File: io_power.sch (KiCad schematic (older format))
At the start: 21 parts, among them U11 TPS7A7100, U12 TPS7A7100, U5 TCA6424A, U6 TPS7A7100

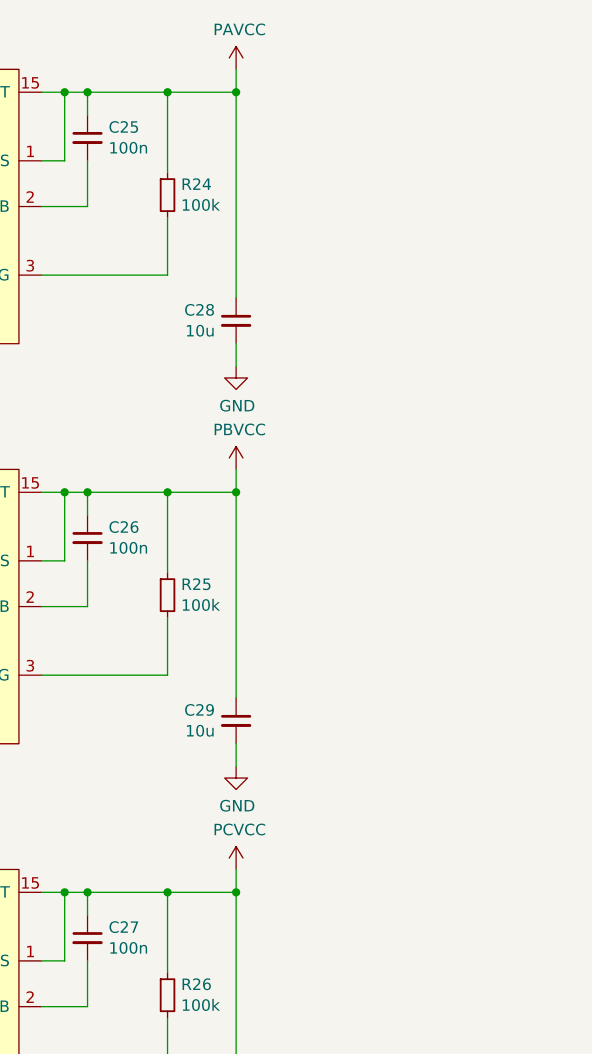
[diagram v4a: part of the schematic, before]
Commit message: Misc silk fixes and add power header
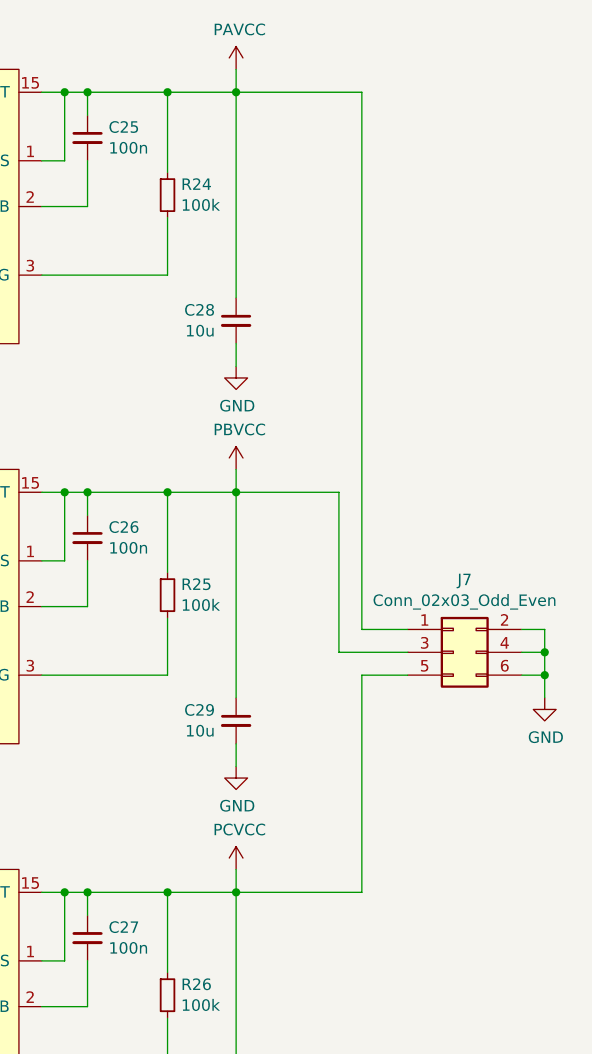
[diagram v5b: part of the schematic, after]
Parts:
- added J7: Conn_02x03_Odd_Even, Connector_PinHeader_2.54mm:PinHeader_2x03_P2.54mm_Vertical, symbol Connector_Generic:Conn_02x03_Odd_Even
- U11, U12, U6: footprint Package_DFN_QFN:VQFN-16-1EP_3x3mm_P0.5mm_EP1.6x1.6mm_ThermalVias -> antboard:VQFN-16-1EP_3x3mm_P0.5mm_EP1.6x1.6mm_ThermalVias
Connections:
- net GND: now also J7.2 (Pin_2), J7.4 (Pin_4), J7.6 (Pin_6)
- net PAVCC: now also J7.1 (Pin_1)
- net PBVCC: now also J7.3 (Pin_3)
- net PCVCC: now also J7.5 (Pin_5)
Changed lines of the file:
@@
 F 0 "U6" H 8000 1265 50  0000 C CNN
 F 1 "TPS7A7100" H 8000 1174 50  0000 C CNN
-F 2 "Package_DFN_QFN:VQFN-16-1EP_3x3mm_P0.5mm_EP1.6x1.6mm_ThermalVias" H 7650 1100 50  0001 C CNN
+F 2 "antboard:VQFN-16-1EP_3x3mm_P0.5mm_EP1.6x1.6mm_ThermalVias" H 7650 1100 50  0001 C CNN
 F 3 "https://www.ti.com/lit/ds/symlink/tps7a7100.pdf" H 7650 1100 50  0001 C CNN
 	1    7650 1100
@@
 F 0 "U11" H 8000 3015 50  0000 C CNN
 F 1 "TPS7A7100" H 8000 2924 50  0000 C CNN
-F 2 "Package_DFN_QFN:VQFN-16-1EP_3x3mm_P0.5mm_EP1.6x1.6mm_ThermalVias" H 7650 2850 50  0001 C CNN
+F 2 "antboard:VQFN-16-1EP_3x3mm_P0.5mm_EP1.6x1.6mm_ThermalVias" H 7650 2850 50  0001 C CNN
 F 3 "https://www.ti.com/lit/ds/symlink/tps7a7100.pdf" H 7650 2850 50  0001 C CNN
 	1    7650 2850
@@
 F 0 "U12" H 8000 4765 50  0000 C CNN
 F 1 "TPS7A7100" H 8000 4674 50  0000 C CNN
-F 2 "Package_DFN_QFN:VQFN-16-1EP_3x3mm_P0.5mm_EP1.6x1.6mm_ThermalVias" H 7650 4600 50  0001 C CNN
+F 2 "antboard:VQFN-16-1EP_3x3mm_P0.5mm_EP1.6x1.6mm_ThermalVias" H 7650 4600 50  0001 C CNN
 F 3 "https://www.ti.com/lit/ds/symlink/tps7a7100.pdf" H 7650 4600 50  0001 C CNN
 	1    7650 4600
@@
 NoConn ~ 4500 4650
 NoConn ~ 4500 4750
+$Comp
+L Connector_Generic:Conn_02x03_Odd_Even J7
+U 1 1 5E0E1804
+P 10250 3650
+F 0 "J7" H 10300 3967 50  0000 C CNN
+F 1 "Conn_02x03_Odd_Even" H 10300 3876 50  0000 C CNN
+F 2 "Connector_PinHeader_2.54mm:PinHeader_2x03_P2.54mm_Vertical" H 10250 3650 50  0001 C CNN
+F 3 "~" H 10250 3650 50  0001 C CNN
+	1    10250 3650
+	1    0    0    -1
+$EndComp
+$Comp
+L power:GND #PWR?
+U 1 1 5E0E2934
+P 10650 3850
+AR Path="/5E0E2934" Ref="#PWR?"  Part="1"
+AR Path="/5DF7E971/5E0E2934" Ref="#PWR?"  Part="1"
+AR Path="/5DFC2583/5E0E2934" Ref="#PWR?"  Part="1"
+AR Path="/5EA8F1AB/5E0E2934" Ref="#PWR047"  Part="1"
+F 0 "#PWR047" H 10650 3600 50  0001 C CNN
+F 1 "GND" H 10655 3677 50  0000 C CNN
+F 2 "" H 10650 3850 50  0001 C CNN
+F 3 "" H 10650 3850 50  0001 C CNN
+	1    10650 3850
+	1    0    0    -1
+$EndComp
+Wire Wire Line
+	10550 3550 10650 3550
+Wire Wire Line
+	10650 3550 10650 3650
+Wire Wire Line
+	10550 3650 10650 3650
+Connection ~ 10650 3650
+Wire Wire Line
+	10650 3650 10650 3750
+Wire Wire Line
+	10550 3750 10650 3750
+Connection ~ 10650 3750
+Wire Wire Line
+	10650 3750 10650 3850
+Wire Wire Line
+	10050 3550 9850 3550
+Wire Wire Line
+	9850 3550 9850 1200
+Wire Wire Line
+	9850 1200 9300 1200
+Wire Wire Line
+	9300 2950 9750 2950
+Wire Wire Line
+	9750 2950 9750 3650
+Wire Wire Line
+	9750 3650 10050 3650
+Wire Wire Line
+	9300 4700 9850 4700
+Wire Wire Line
+	9850 4700 9850 3750
+Wire Wire Line
+	9850 3750 10050 3750
 $EndSCHEMATC

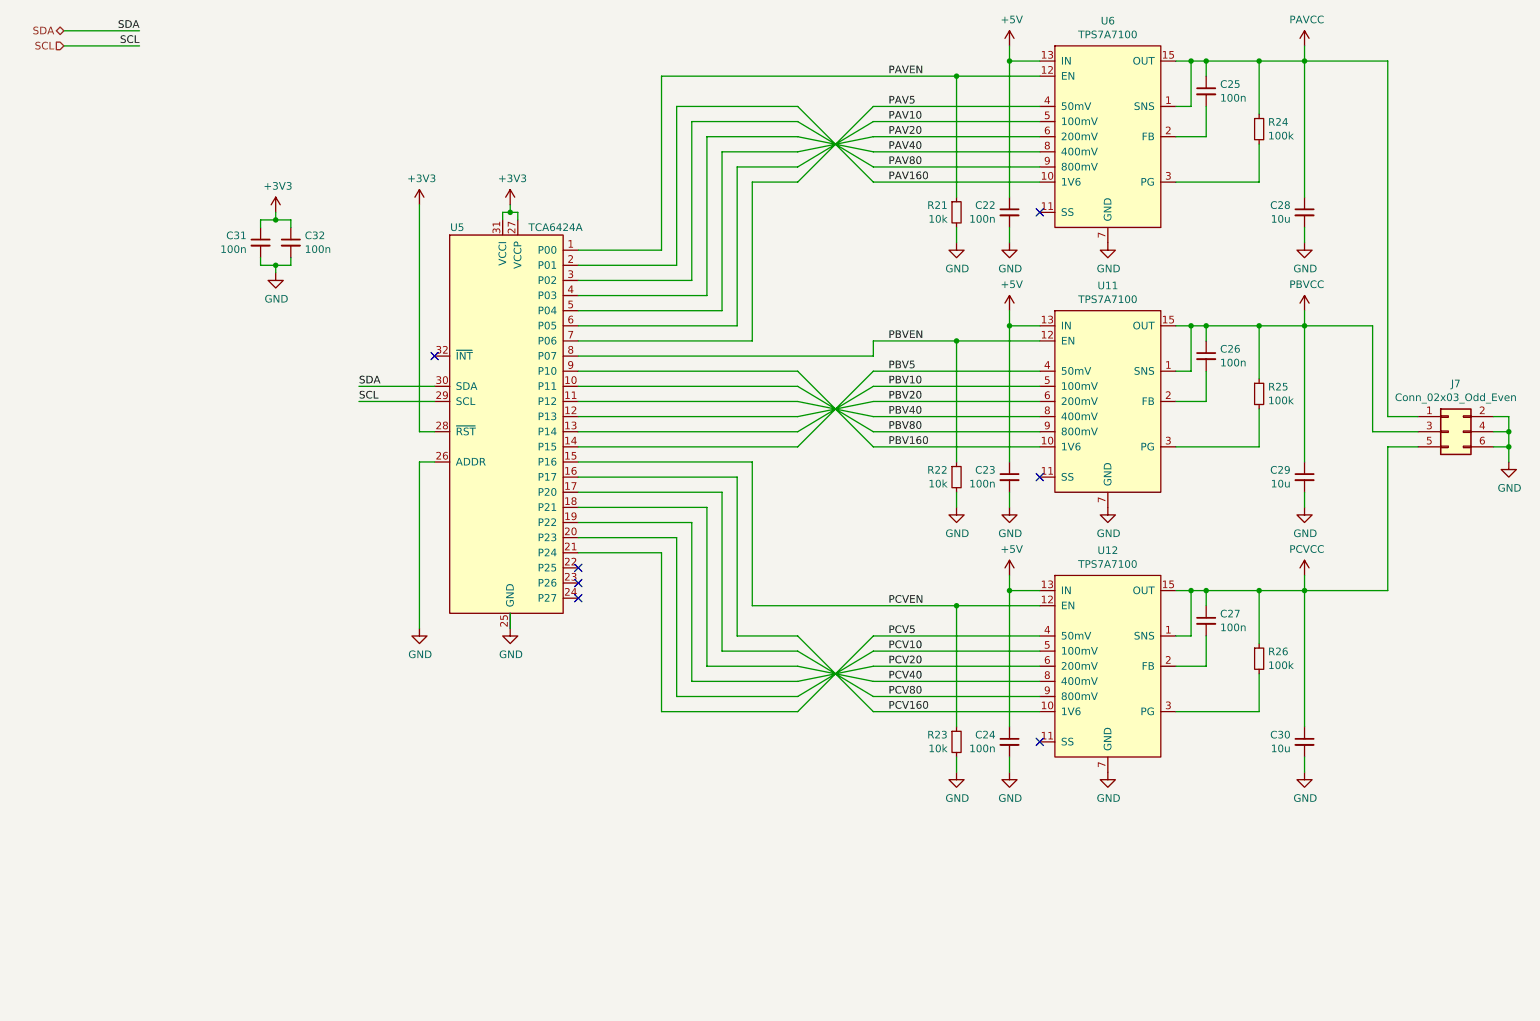
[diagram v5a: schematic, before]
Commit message: sch, pcb: Add ADC to read set IO voltages
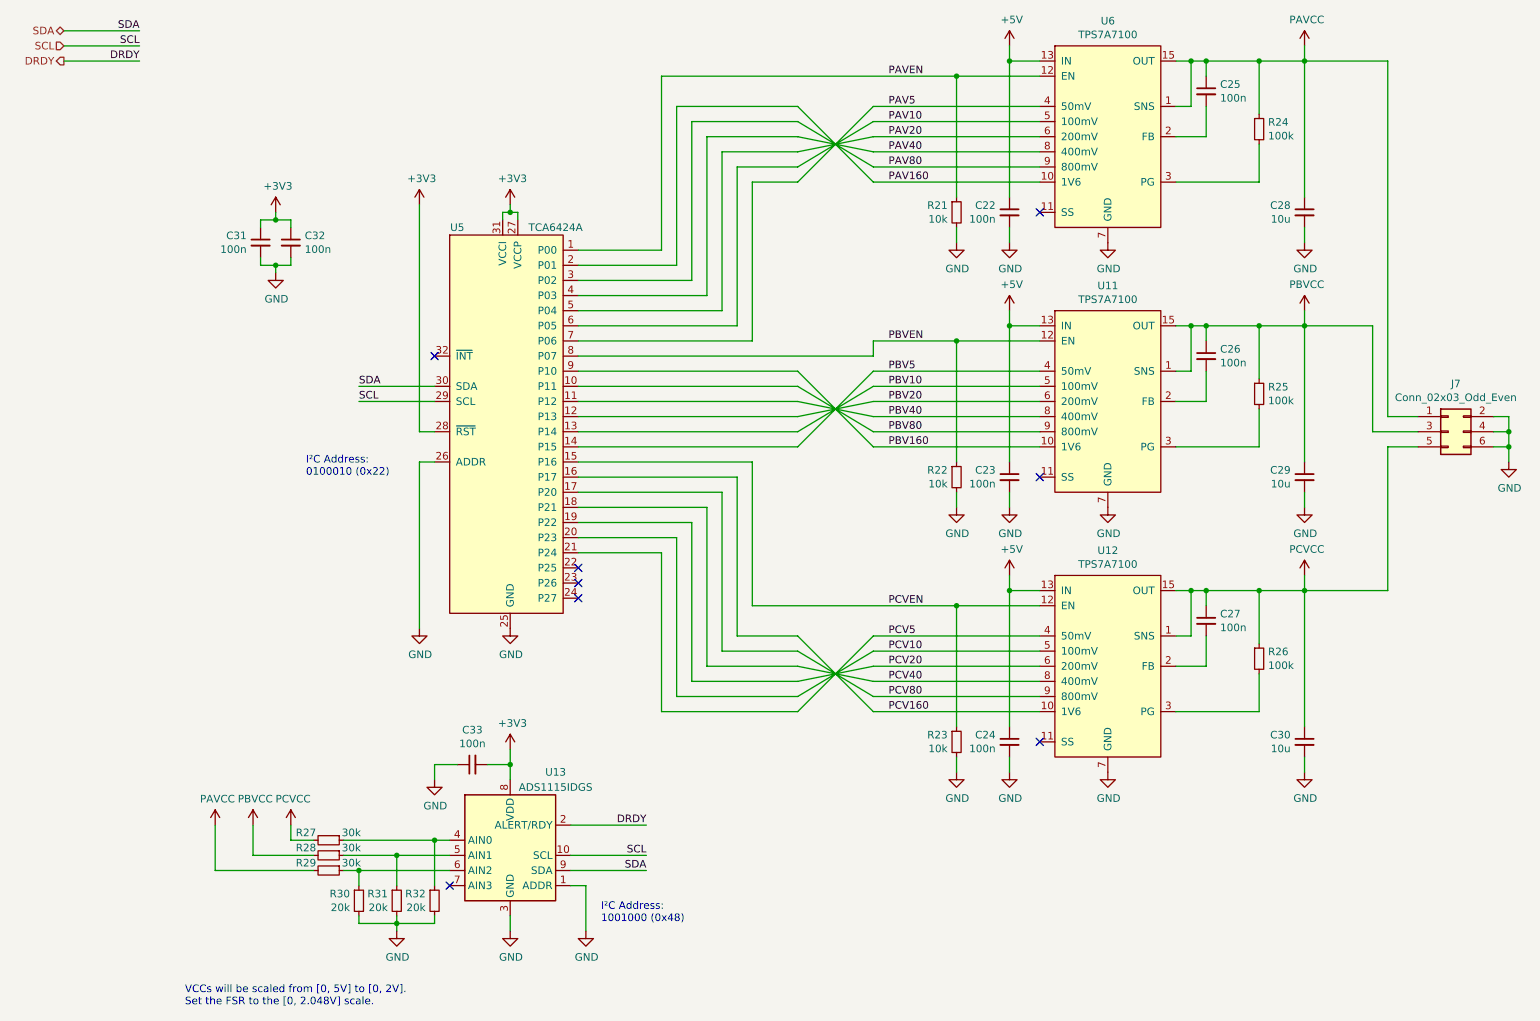
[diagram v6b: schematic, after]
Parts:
- added C33: 100n, Capacitor_SMD:C_0603_1608Metric, symbol Device:C_Small
- added R27, R28, R29: 30k, Resistor_SMD:R_0603_1608Metric, symbol Device:R_Small
- added R30, R31, R32: 20k, Resistor_SMD:R_0603_1608Metric, symbol Device:R_Small
- added U13: ADS1115IDGS, Package_SO:TSSOP-10_3x3mm_P0.5mm, symbol Analog_ADC:ADS1115IDGS
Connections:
- net +3V3: now also C33.2, U13.8 (VDD)
- net GND: now also C33.1, R30.2, R31.2, R32.2, U13.1 (ADDR), U13.3 (GND)
- net PAVCC: now also R29.2
- net PBVCC: now also R28.2
- net PCVCC: now also R27.2
- net SCL: now also U13.10 (SCL)
- net SDA: now also U13.9 (SDA)
- new net: R27.1, R32.1, U13.4 (AIN0)
- new net: R28.1, R31.1, U13.5 (AIN1)
- new net: R29.1, R30.1, U13.6 (AIN2)
- new net DRDY: U13.2 (ALERT/RDY)
- no-connect marks 7 -> 8
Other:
- note added: "I²C Address:\n0100010 (0x22)"
- note added: "I²C Address:\n1001000 (0x48)"
- note added: "VCCs will be scaled from [0, 5V] to [0, 2V].\nSet the FSR to the [0, 2.048V] scale."
